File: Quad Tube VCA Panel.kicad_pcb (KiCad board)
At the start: 2 copper layers, 162.6 x 128.5 mm, 0 parts

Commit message: updates panel copper/silkscreen again
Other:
- board text added: "[HardWired Engineering]"
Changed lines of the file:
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@@
     (effects (font (size 3 3) (thickness 0.3)))
   )
-  (gr_text "HardWired Engineering" (at 88.011 185.42) (layer F.SilkS)
+  (gr_text "[HardWired Engineering]" (at 88.011 185.42) (layer F.SilkS)
     (effects (font (size 2.5 2.5) (thickness 0.25)))
   )

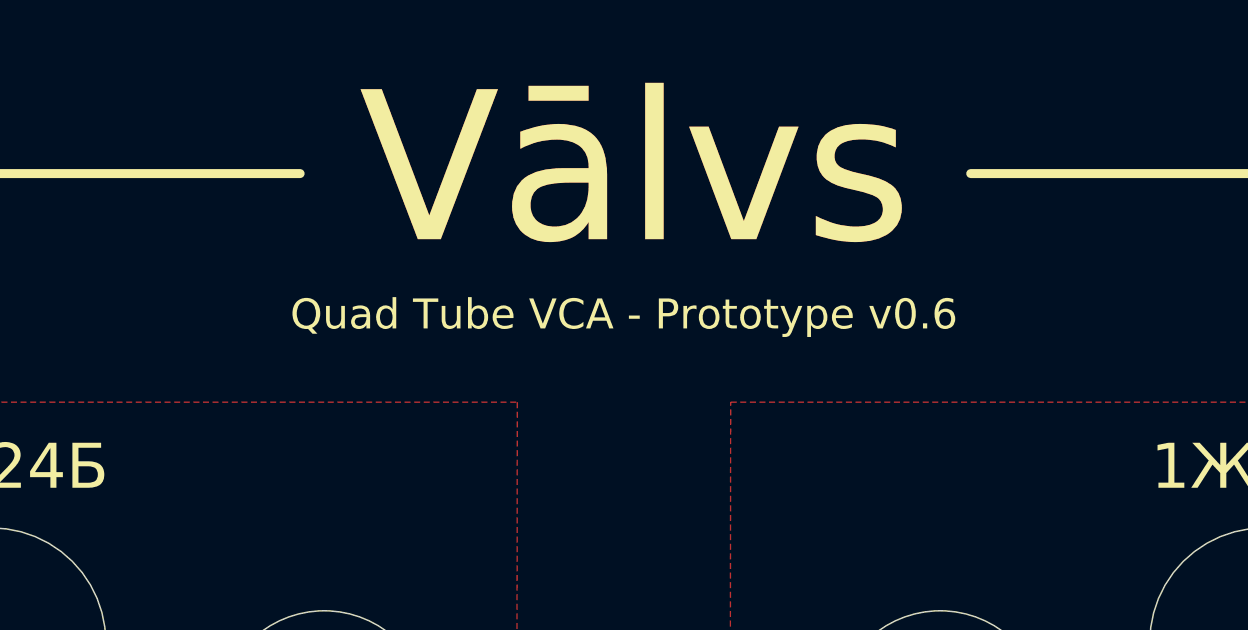
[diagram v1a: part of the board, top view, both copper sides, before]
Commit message: reroutes pots on PCB
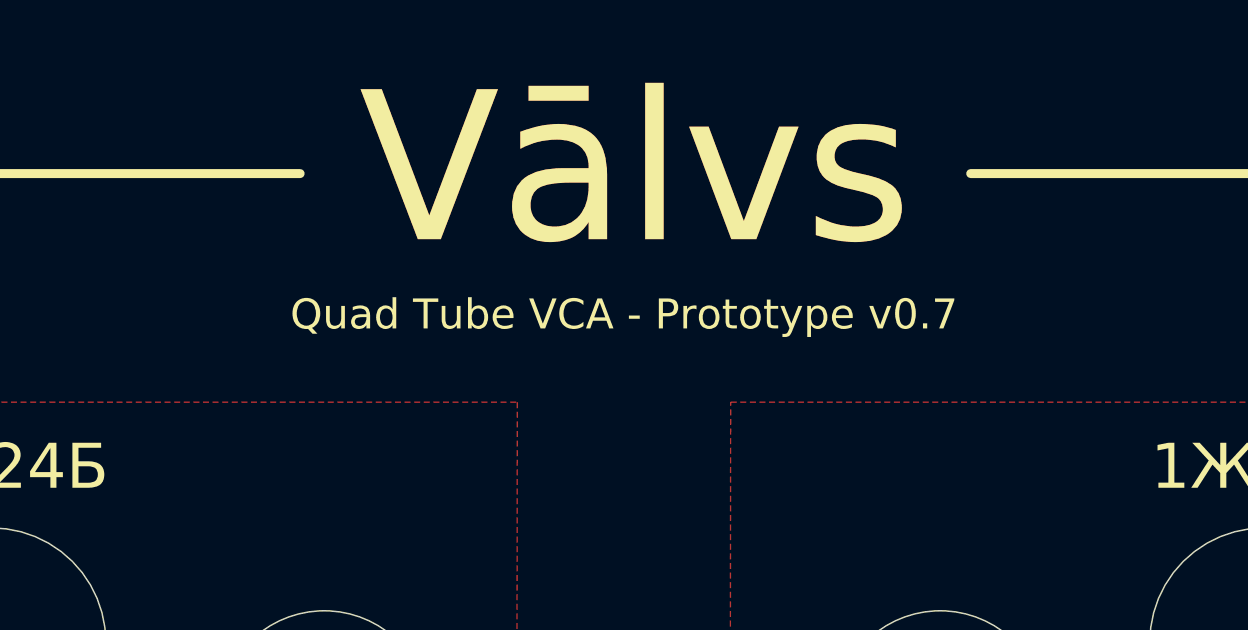
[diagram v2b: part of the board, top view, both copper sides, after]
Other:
- board text added: "Quad Tube VCA - Prototype v0.7"
- board text removed: "Quad Tube VCA - Prototype v0.6"
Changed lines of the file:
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@@
     (effects (font (size 2 2) (thickness 0.2)))
   )
-  (gr_text "Quad Tube VCA - Prototype v0.6" (at 87.757 73.787) (layer F.SilkS)
+  (gr_text "Quad Tube VCA - Prototype v0.7" (at 87.757 73.787) (layer F.SilkS)
     (effects (font (size 1 1) (thickness 0.15)))
   )

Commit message: adds new images
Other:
- board text added: "C L E A N"
- board text added: "D I R T Y"
- board text added: "Q U A D T U B E V C A"
- board text removed: "Clean"
- board text removed: "Dirt"
- board text removed: "Quad Tube VCA - Prototype v0.7"

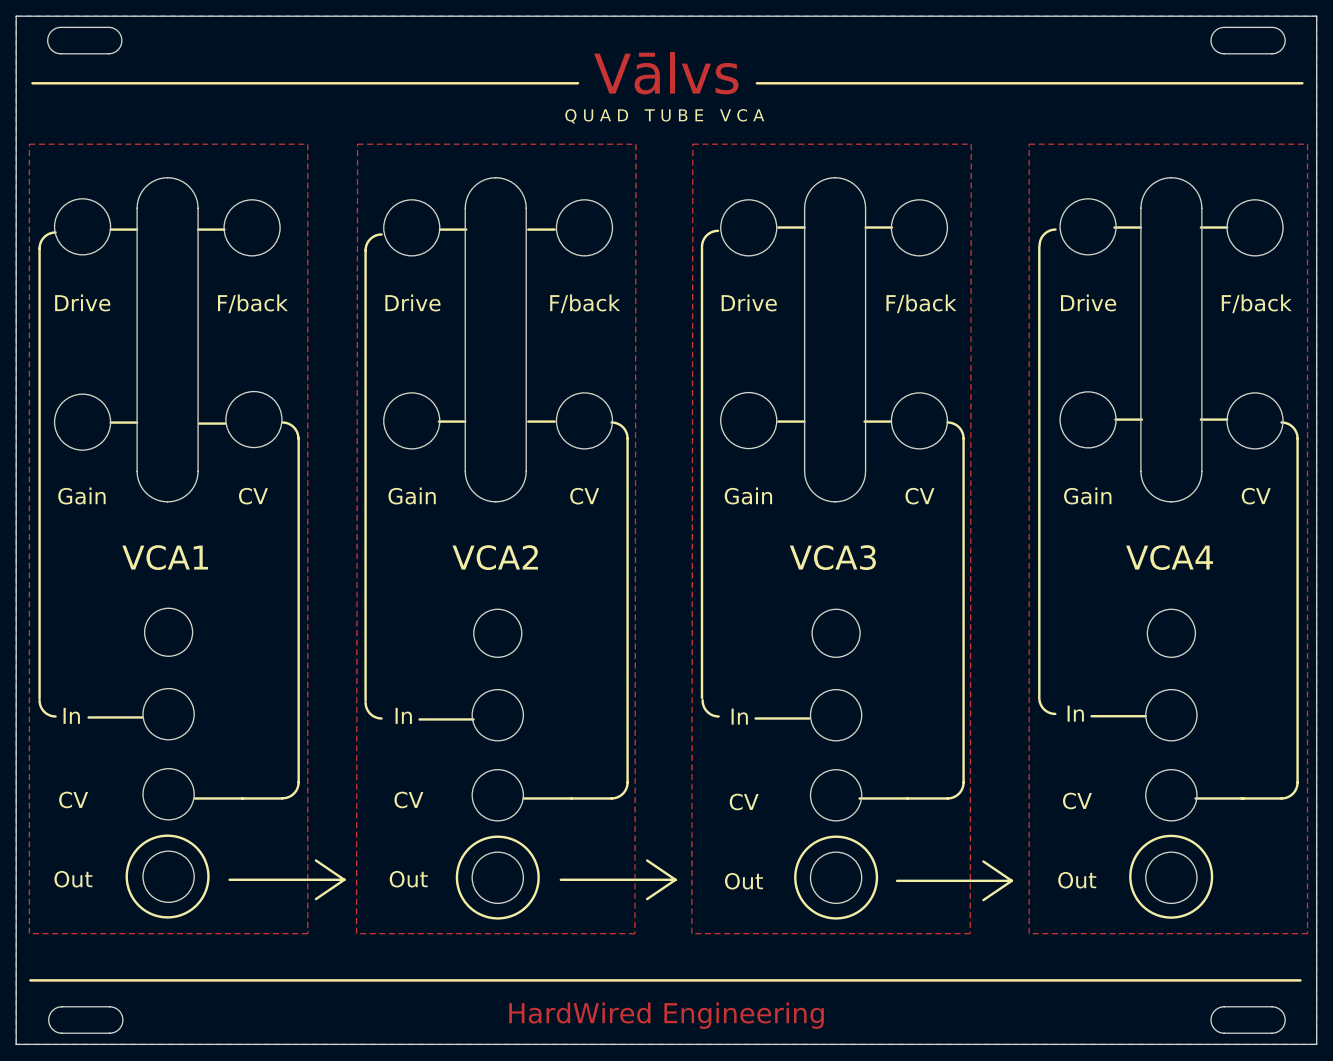
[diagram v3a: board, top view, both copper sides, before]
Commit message: updates panel fonts
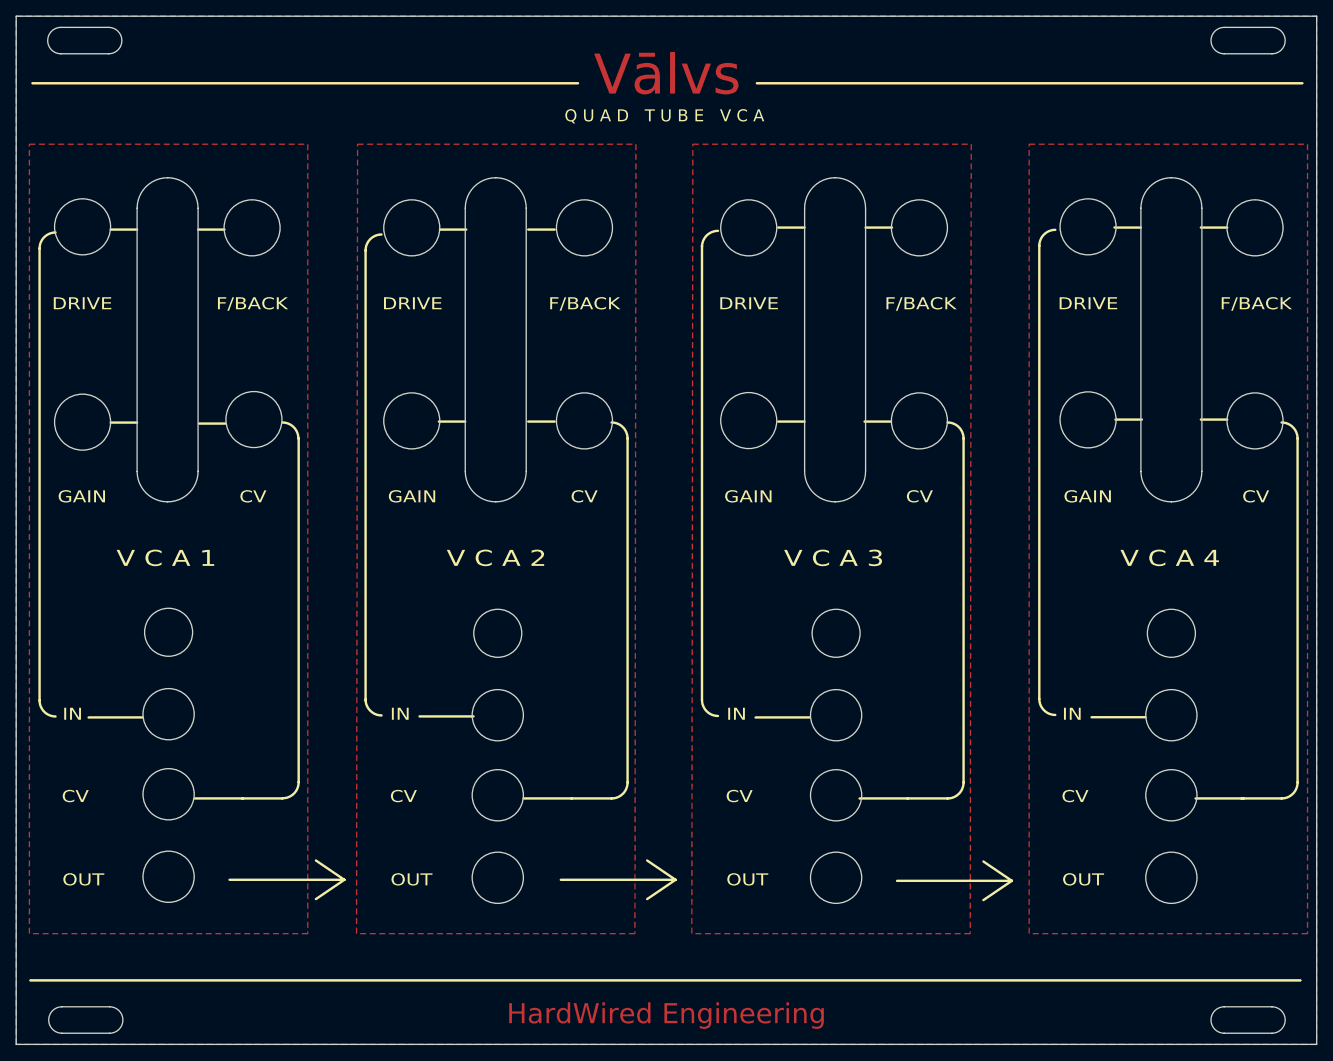
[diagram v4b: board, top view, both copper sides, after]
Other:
- board text added: "DRIVE"
- board text added: "F/BACK"
- board text added: "GAIN"
- board text added: "IN"
- board text added: "OUT"
- board text added: "V C A 1"
- board text added: "V C A 2"
- board text added: "V C A 3"
- board text added: "V C A 4"
- board text removed: "Drive"
- board text removed: "F/back"
- board text removed: "Gain"
- board text removed: "In"
- board text removed: "Out"
- board text removed: "VCA1"
- board text removed: "VCA2"
- board text removed: "VCA3"
- board text removed: "VCA4"

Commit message: updates panel
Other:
- board text added: "[ H A R D W I R E D E N G I N E E R I N G ]"
- board text removed: "HardWired Engineering"
- board text removed: "[HardWired Engineering]"
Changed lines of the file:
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@@
     (uvia_drill 0.1)
+  )
+  (gr_text "[ H A R D W I R E D   E N G I N E E R I N G ]" (at 88.011 185.42) (layer F.Cu)
+    (effects (font (size 1 1.5) (thickness 0.25)))
   )
   (gr_line (start 134.62 145.785) (end 134.62 146.05) (layer F.SilkS) (width 0.12))
@@
   (gr_circle (center 66.929 168.376663) (end 72.034337 168.376663) (layer F.Mask) (width 0.3))
   (gr_circle (center 25.654 168.249663) (end 30.759337 168.249663) (layer F.Mask) (width 0.3))
-  (gr_text "HardWired Engineering" (at 88.011 185.42) (layer F.Cu)
-    (effects (font (size 2.5 2.5) (thickness 0.25)))
-  )
   (gr_text Vālvs (at 88.138 68.072) (layer F.Cu)
     (effects (font (size 5 5) (thickness 0.5)))
@@
     (effects (font (size 2 2.5) (thickness 0.3)))
   )
-  (gr_text "[HardWired Engineering]" (at 88.011 185.42) (layer F.Mask)
-    (effects (font (size 2.5 2.5) (thickness 0.25)))
+  (gr_text "[ H A R D W I R E D   E N G I N E E R I N G ]" (at 88.011 185.42) (layer F.Mask)
+    (effects (font (size 1 1.5) (thickness 0.25)))
   )
   (gr_text 1Ж24Б (at 25.654 78.867) (layer F.Mask)
